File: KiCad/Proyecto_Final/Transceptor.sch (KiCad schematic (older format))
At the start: 51 parts, among them J2 ADC_CLK_SEL, T3 2450BL05A0100, U10 MAX2837, U9 MAX1193ETI+

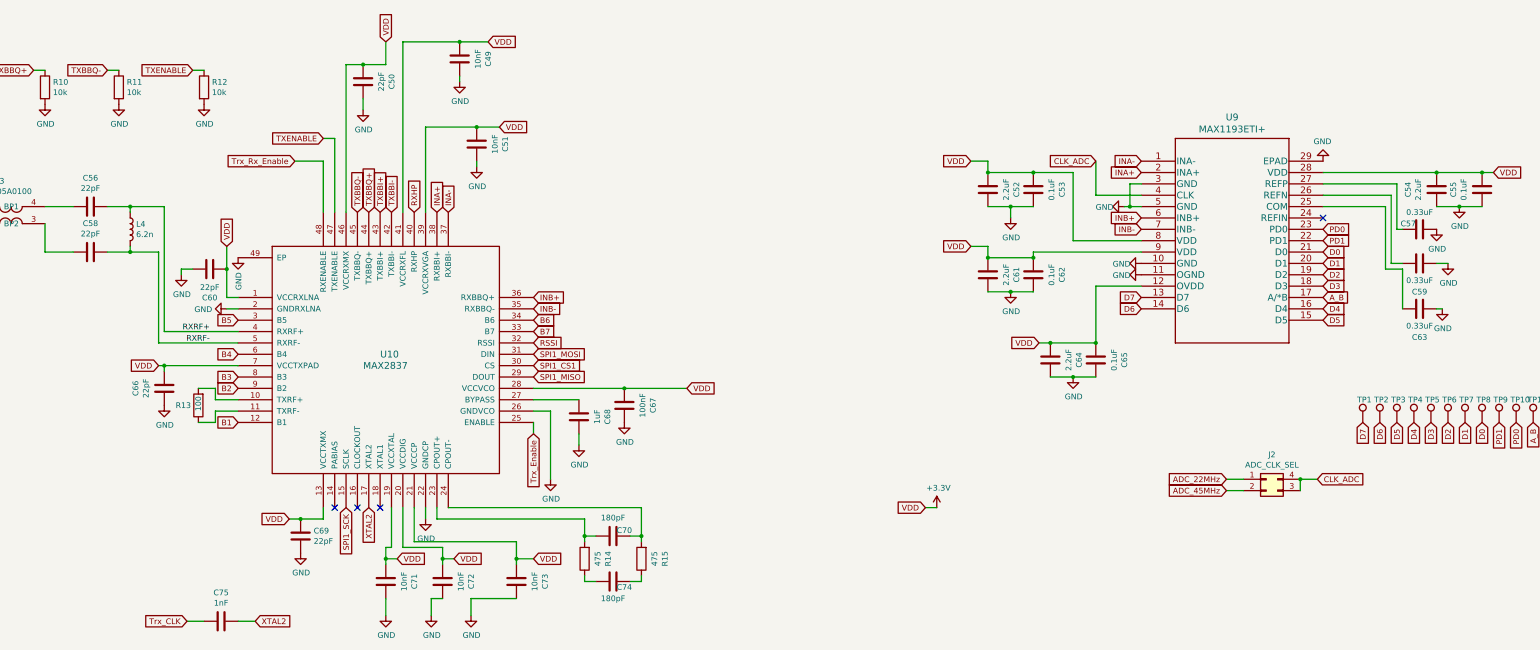
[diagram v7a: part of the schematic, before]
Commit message: PCB Frontend terminado y empezado parte Transceptor.
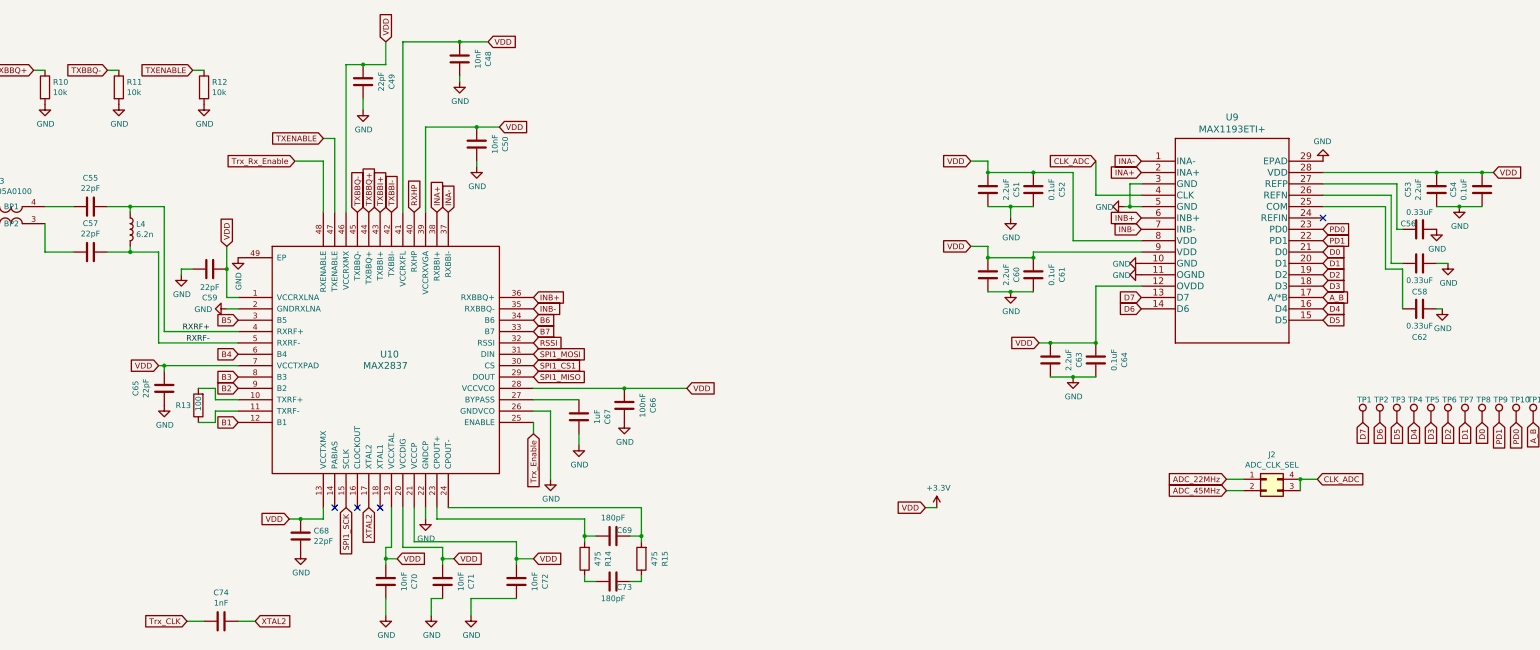
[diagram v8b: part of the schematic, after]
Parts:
- renumbered C49 to C48, C50 to C49, C51 to C50, C52 to C51, C53 to C52, C54 to C53, C55 to C54, C56 to C55, C57 to C56, C58 to C57, C59 to C58, C60 to C59, C61 to C60, C62 to C61, C63 to C62, C64 to C63, C65 to C64, C66 to C65, C67 to C66, C68 to C67, C69 to C68, C70 to C69, C71 to C70, C72 to C71, C73 to C72, C74 to C73, C75 to C74
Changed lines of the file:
@@
 $EndComp
 $Comp
-L Device:C C56
+L Device:C C55
 U 1 1 5FDD636C
 P 3050 2350
-F 0 "C56" V 2798 2350 50  0000 C CNN
+F 0 "C55" V 2798 2350 50  0000 C CNN
 F 1 "22pF" V 2889 2350 50  0000 C CNN
 F 2 "Capacitor_SMD:C_0402_1005Metric" H 3088 2200 50  0001 C CNN
@@
 $EndComp
 $Comp
-L Device:C C58
+L Device:C C57
 U 1 1 5FDD6D2A
 P 3050 2750
-F 0 "C58" V 2798 2750 50  0000 C CNN
+F 0 "C57" V 2798 2750 50  0000 C CNN
 F 1 "22pF" V 2889 2750 50  0000 C CNN
 F 2 "Capacitor_SMD:C_0402_1005Metric" H 3088 2600 50  0001 C CNN
@@
 Connection ~ 3400 2750
 $Comp
-L Device:C C60
+L Device:C C59
 U 1 1 5FF7A13F
 P 4100 2900
-F 0 "C60" V 3848 2900 50  0000 C CNN
+F 0 "C59" V 3848 2900 50  0000 C CNN
 F 1 "22pF" V 3939 2900 50  0000 C CNN
 F 2 "Capacitor_SMD:C_0402_1005Metric" H 4138 2750 50  0001 C CNN
@@
 	4250 2900 4250 3150
 $Comp
-L Device:C C66
+L Device:C C65
 U 1 1 602785CE
 P 3700 3950
-F 0 "C66" V 3448 3950 50  0000 C CNN
+F 0 "C65" V 3448 3950 50  0000 C CNN
 F 1 "22pF" V 3539 3950 50  0000 C CNN
 F 2 "Capacitor_SMD:C_0402_1005Metric" H 3738 3800 50  0001 C CNN
@@
 SPI1_SCK
 $Comp
-L Device:C C71
+L Device:C C70
 U 1 1 602E954C
 P 5650 5650
-F 0 "C71" V 5398 5650 50  0000 C CNN
+F 0 "C70" V 5398 5650 50  0000 C CNN
 F 1 "10nF" V 5489 5650 50  0000 C CNN
 F 2 "Capacitor_SMD:C_0402_1005Metric" H 5688 5500 50  0001 C CNN
@@
 	5650 5450 5650 5500
 $Comp
-L Device:C C72
+L Device:C C71
 U 1 1 602F4DEF
 P 6150 5650
-F 0 "C72" V 5898 5650 50  0000 C CNN
+F 0 "C71" V 5898 5650 50  0000 C CNN
 F 1 "10nF" V 5989 5650 50  0000 C CNN
 F 2 "Capacitor_SMD:C_0402_1005Metric" H 6188 5500 50  0001 C CNN
@@
 	6150 5800 6050 5800
 $Comp
-L Device:C C73
+L Device:C C72
 U 1 1 60305E98
 P 6800 5650
-F 0 "C73" V 6548 5650 50  0000 C CNN
+F 0 "C72" V 6548 5650 50  0000 C CNN
 F 1 "10nF" V 6639 5650 50  0000 C CNN
 F 2 "Capacitor_SMD:C_0402_1005Metric" H 6838 5500 50  0001 C CNN
@@
 	6000 5100 6000 5000
 $Comp
-L Device:C C70
+L Device:C C69
 U 1 1 603215A5
 P 7650 5250
-F 0 "C70" V 7600 5350 50  0000 C CNN
+F 0 "C69" V 7600 5350 50  0000 C CNN
 F 1 "180pF" V 7489 5250 50  0000 C CNN
 F 2 "Capacitor_SMD:C_0402_1005Metric" H 7688 5100 50  0001 C CNN
@@
 $EndComp
 $Comp
-L Device:C C74
+L Device:C C73
 U 1 1 6032557A
 P 7650 5650
-F 0 "C74" V 7700 5750 50  0000 C CNN
+F 0 "C73" V 7700 5750 50  0000 C CNN
 F 1 "180pF" V 7800 5650 50  0000 C CNN
 F 2 "Capacitor_SMD:C_0402_1005Metric" H 7688 5500 50  0001 C CNN
@@
 	7100 4150 6950 4150
 $Comp
-L Device:C C68
+L Device:C C67
 U 1 1 60348680
 P 7350 4200
-F 0 "C68" V 7098 4200 50  0000 C CNN
+F 0 "C67" V 7098 4200 50  0000 C CNN
 F 1 "1uF" V 7189 4200 50  0000 C CNN
 F 2 "Capacitor_SMD:C_0805_2012Metric" H 7388 4050 50  0001 C CNN
@@
 	7350 4450 7350 4350
 $Comp
-L Device:C C67
+L Device:C C66
 U 1 1 60351476
 P 7750 4100
-F 0 "C67" V 7498 4100 50  0000 C CNN
+F 0 "C66" V 7498 4100 50  0000 C CNN
 F 1 "100nF" V 7589 4100 50  0000 C CNN
 F 2 "Capacitor_SMD:C_0402_1005Metric" H 7788 3950 50  0001 C CNN
@@
 RSSI
 $Comp
-L Device:C C51
+L Device:C C50
 U 1 1 603DBC76
 P 6450 1800
-F 0 "C51" V 6198 1800 50  0000 C CNN
+F 0 "C50" V 6198 1800 50  0000 C CNN
 F 1 "10nF" V 6289 1800 50  0000 C CNN
 F 2 "Capacitor_SMD:C_0402_1005Metric" H 6488 1650 50  0001 C CNN
@@
 VDD
 $Comp
-L Device:C C49
+L Device:C C48
 U 1 1 603F8A2A
 P 6300 1050
-F 0 "C49" V 6048 1050 50  0000 C CNN
+F 0 "C48" V 6048 1050 50  0000 C CNN
 F 1 "10nF" V 6139 1050 50  0000 C CNN
 F 2 "Capacitor_SMD:C_0402_1005Metric" H 6338 900 50  0001 C CNN
@@
 Connection ~ 6300 900
 $Comp
-L Device:C C50
+L Device:C C49
 U 1 1 6040CEDC
 P 5450 1250
-F 0 "C50" V 5198 1250 50  0000 C CNN
+F 0 "C49" V 5198 1250 50  0000 C CNN
 F 1 "22pF" V 5289 1250 50  0000 C CNN
 F 2 "Capacitor_SMD:C_0402_1005Metric" H 5488 1100 50  0001 C CNN
@@
 	11350 2050 10950 2050
 $Comp
-L Device:C C53
+L Device:C C52
 U 1 1 6035F275
 P 11350 2200
-F 0 "C53" V 11098 2200 50  0000 C CNN
+F 0 "C52" V 11098 2200 50  0000 C CNN
 F 1 "0.1uF" V 11189 2200 50  0000 C CNN
 F 2 "Capacitor_SMD:C_0402_1005Metric" H 11388 2050 50  0001 C CNN
@@
 Connection ~ 10950 2050
 $Comp
-L Device:C C52
+L Device:C C51
 U 1 1 6035E627
 P 10950 2200
-F 0 "C52" V 10698 2200 50  0000 C CNN
+F 0 "C51" V 10698 2200 50  0000 C CNN
 F 1 "2.2uF" V 10789 2200 50  0000 C CNN
 F 2 "Capacitor_SMD:C_0805_2012Metric" H 10988 2050 50  0001 C CNN
@@
 Connection ~ 11350 2050
 $Comp
-L Device:C C61
+L Device:C C60
 U 1 1 6041305D
 P 10950 2950
-F 0 "C61" V 10698 2950 50  0000 C CNN
+F 0 "C60" V 10698 2950 50  0000 C CNN
 F 1 "2.2uF" V 10789 2950 50  0000 C CNN
 F 2 "Capacitor_SMD:C_0805_2012Metric" H 10988 2800 50  0001 C CNN
@@
 $EndComp
 $Comp
-L Device:C C62
+L Device:C C61
 U 1 1 60413718
 P 11350 2950
-F 0 "C62" V 11098 2950 50  0000 C CNN
+F 0 "C61" V 11098 2950 50  0000 C CNN
 F 1 "0.1uF" V 11189 2950 50  0000 C CNN
 F 2 "Capacitor_SMD:C_0402_1005Metric" H 11388 2800 50  0001 C CNN
@@
 $EndComp
 $Comp
-L Device:C C64
+L Device:C C63
 U 1 1 6043F388
 P 11500 3700
-F 0 "C64" V 11248 3700 50  0000 C CNN
+F 0 "C63" V 11248 3700 50  0000 C CNN
 F 1 "2.2uF" V 11339 3700 50  0000 C CNN
 F 2 "Capacitor_SMD:C_0805_2012Metric" H 11538 3550 50  0001 C CNN
@@
 Connection ~ 11900 3550
 $Comp
-L Device:C C65
+L Device:C C64
 U 1 1 6043FA03
 P 11900 3700
-F 0 "C65" V 11648 3700 50  0000 C CNN
+F 0 "C64" V 11648 3700 50  0000 C CNN
 F 1 "0.1uF" V 11739 3700 50  0000 C CNN
 F 2 "Capacitor_SMD:C_0402_1005Metric" H 11938 3550 50  0001 C CNN
@@
 $EndComp
 $Comp
-L Device:C C55
+L Device:C C54
 U 1 1 604785CC
 P 15300 2200
-F 0 "C55" V 15048 2200 50  0000 C CNN
+F 0 "C54" V 15048 2200 50  0000 C CNN
 F 1 "0.1uF" V 15139 2200 50  0000 C CNN
 F 2 "Capacitor_SMD:C_0402_1005Metric" H 15338 2050 50  0001 C CNN
@@
 $EndComp
 $Comp
-L Device:C C54
+L Device:C C53
 U 1 1 604798D7
 P 14900 2200
-F 0 "C54" V 14648 2200 50  0000 C CNN
+F 0 "C53" V 14648 2200 50  0000 C CNN
 F 1 "2.2uF" V 14739 2200 50  0000 C CNN
 F 2 "Capacitor_SMD:C_0805_2012Metric" H 14938 2050 50  0001 C CNN
@@
 Connection ~ 14900 2050
 $Comp
-L Device:C C57
+L Device:C C56
 U 1 1 6049FB43
 P 14750 2550
-F 0 "C57" V 14800 2650 50  0000 C CNN
+F 0 "C56" V 14800 2650 50  0000 C CNN
 F 1 "0.33uF" V 14900 2550 50  0000 C CNN
 F 2 "Capacitor_SMD:C_0603_1608Metric" H 14788 2400 50  0001 C CNN
@@
 $EndComp
 $Comp
-L Device:C C59
+L Device:C C58
 U 1 1 604A0B95
 P 14750 2850
-F 0 "C59" V 15000 2850 50  0000 C CNN
+F 0 "C58" V 15000 2850 50  0000 C CNN
 F 1 "0.33uF" V 14900 2850 50  0000 C CNN
 F 2 "Capacitor_SMD:C_0603_1608Metric" H 14788 2700 50  0001 C CNN
@@
 	14500 2850 14500 2250
 $Comp
-L Device:C C63
+L Device:C C62
 U 1 1 60505AC2
 P 14750 3250
-F 0 "C63" V 15000 3250 50  0000 C CNN
+F 0 "C62" V 15000 3250 50  0000 C CNN
 F 1 "0.33uF" V 14900 3250 50  0000 C CNN
 F 2 "Capacitor_SMD:C_0603_1608Metric" H 14788 3100 50  0001 C CNN
@@
 $EndComp
 $Comp
-L Device:C C69
+L Device:C C68
 U 1 1 60750C4A
 P 4900 5250
-F 0 "C69" H 5015 5296 50  0000 L CNN
+F 0 "C68" H 5015 5296 50  0000 L CNN
 F 1 "22pF" H 5015 5205 50  0000 L CNN
 F 2 "Capacitor_SMD:C_0402_1005Metric" H 4938 5100 50  0001 C CNN
@@
 NoConn ~ 5600 5000
 $Comp
-L Device:C C75
+L Device:C C74
 U 1 1 60782802
 P 4200 6000
-F 0 "C75" V 3948 6000 50  0000 C CNN
+F 0 "C74" V 3948 6000 50  0000 C CNN
 F 1 "1nF" V 4039 6000 50  0000 C CNN
 F 2 "Capacitor_SMD:C_0402_1005Metric" H 4238 5850 50  0001 C CNN
